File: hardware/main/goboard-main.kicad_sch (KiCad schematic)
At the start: 12 parts, among them J1 USB_C_Receptacle_USB2.0, J2 Conn_02x05_Top_Bottom, J3 Conn_01x01, J4 Conn_01x04, SW11 SW_Push

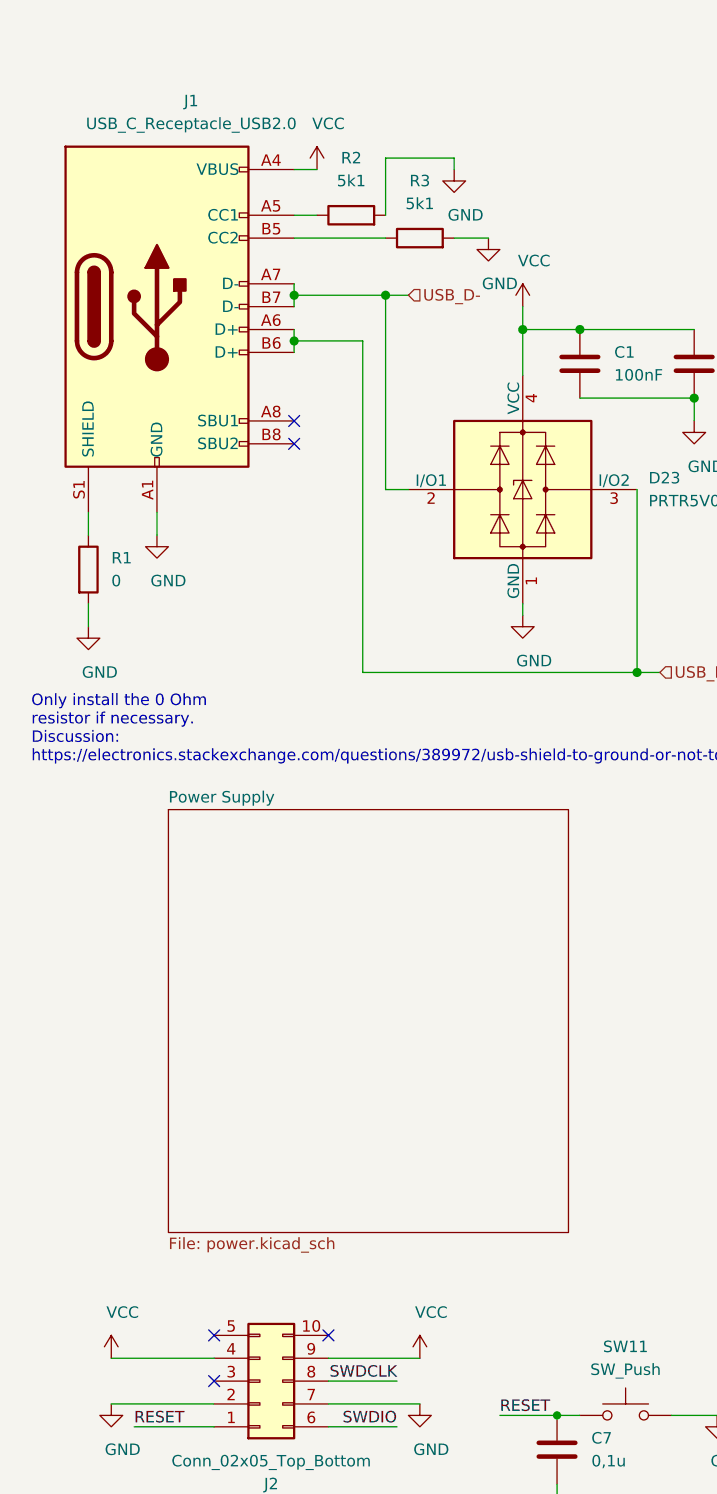
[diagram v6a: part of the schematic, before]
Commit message: Add power supply from the debugging connector
The batteries have to be disconnected when the debugger is plugged in,
as the voltages differ (ca. 2V for the batteries, 3.3V for the
debugger).
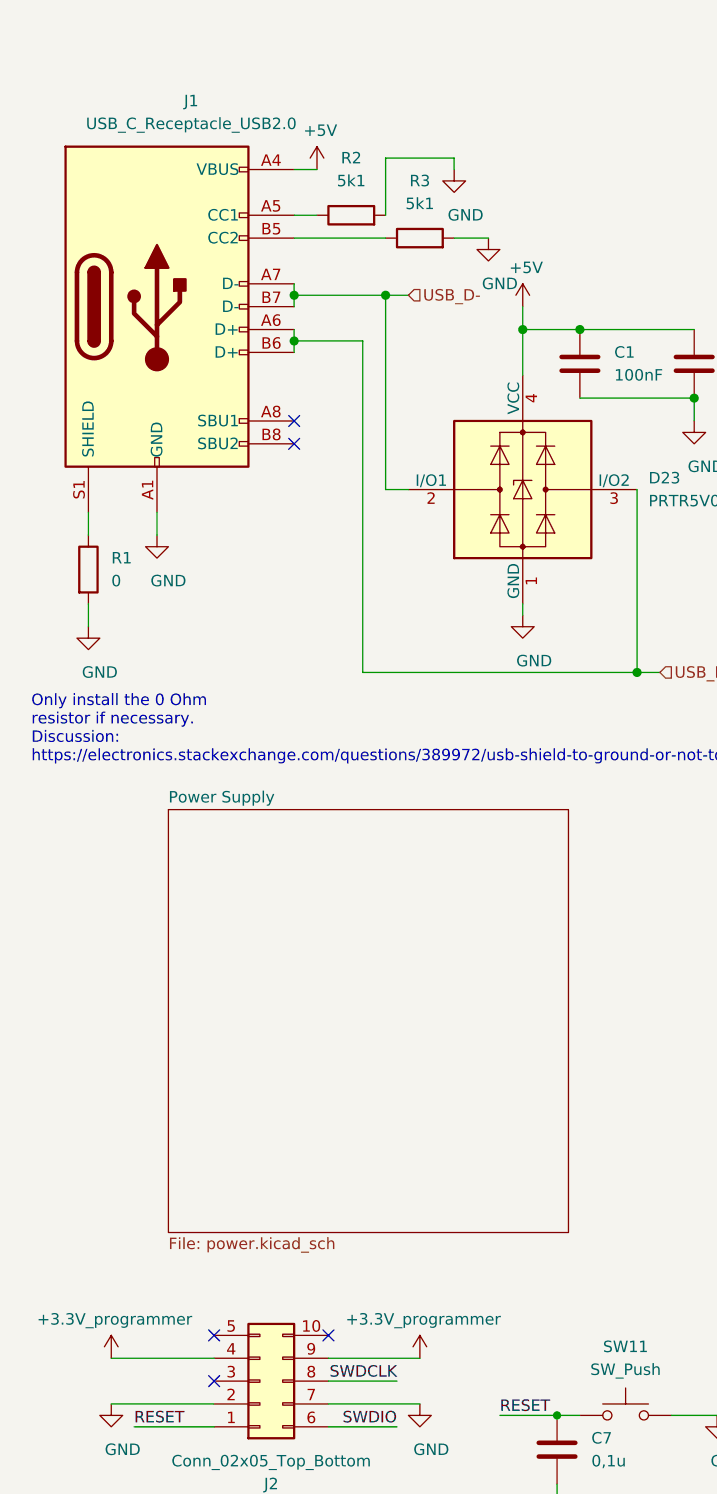
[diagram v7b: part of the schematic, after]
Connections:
- net VCC renamed +5V
- net +5V: no longer J2.4 (Pin_4), J2.9 (Pin_9)
- new net +3V3: J2.4 (Pin_4), J2.9 (Pin_9)
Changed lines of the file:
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@@
   (junction (at 80.01 91.44) (diameter 1.016) (color 0 0 0 0))
   (junction (at 86.36 60.96) (diameter 1.016) (color 0 0 0 0))
+  (no_connect (at 33.02 165.1))
+  (no_connect (at 33.02 170.18))
+  (no_connect (at 41.91 63.5))
   (no_connect (at 41.91 66.04))
   (no_connect (at 45.72 165.1))
-  (no_connect (at 41.91 63.5))
-  (no_connect (at 33.02 170.18))
-  (no_connect (at 33.02 165.1))
   (wire (pts (xy 19.05 73.66) (xy 19.05 76.2))
     (stroke (width 0) (type solid) (color 0 0 0 0))
@@
     (effects (font (size 1.27 1.27)) (justify right))
   )
-  (symbol (lib_id "power:VCC") (at 21.59 167.64 0) (unit 1)
-    (in_bom yes) (on_board yes)
-    (property "Reference" "#PWR0115" (id 0) (at 21.59 171.45 0)
-      (effects (font (size 1.27 1.27)) hide)
-    )
-    (property "Value" "VCC" (id 1) (at 22.86 162.56 0))
+  (symbol (lib_id "power:+3.3V") (at 21.59 167.64 0) (unit 1)
+    (in_bom yes) (on_board yes)
+    (property "Reference" "#PWR?" (id 0) (at 21.59 171.45 0)
+      (effects (font (size 1.27 1.27)) hide)
+    )
+    (property "Value" "+3.3V_programmer" (id 1) (at 21.958 163.316 0))
     (property "Footprint" "" (id 2) (at 21.59 167.64 0)
       (effects (font (size 1.27 1.27)) hide)
@@
     )
   )
-  (symbol (lib_id "power:VCC") (at 44.45 35.56 0) (unit 1)
-    (in_bom yes) (on_board yes)
-    (property "Reference" "#PWR0108" (id 0) (at 44.45 39.37 0)
-      (effects (font (size 1.27 1.27)) hide)
-    )
-    (property "Value" "VCC" (id 1) (at 45.72 30.48 0))
+  (symbol (lib_id "power:+5V") (at 44.45 35.56 0) (unit 1)
+    (in_bom yes) (on_board yes)
+    (property "Reference" "#PWR?" (id 0) (at 44.45 39.37 0)
+      (effects (font (size 1.27 1.27)) hide)
+    )
+    (property "Value" "+5V" (id 1) (at 44.8183 31.2356 0))
     (property "Footprint" "" (id 2) (at 44.45 35.56 0)
       (effects (font (size 1.27 1.27)) hide)
@@
     )
   )
-  (symbol (lib_id "power:VCC") (at 55.88 167.64 0) (unit 1)
-    (in_bom yes) (on_board yes)
-    (property "Reference" "#PWR0116" (id 0) (at 55.88 171.45 0)
-      (effects (font (size 1.27 1.27)) hide)
-    )
-    (property "Value" "VCC" (id 1) (at 57.15 162.56 0))
+  (symbol (lib_id "power:+3.3V") (at 55.88 167.64 0) (unit 1)
+    (in_bom yes) (on_board yes)
+    (property "Reference" "#PWR?" (id 0) (at 55.88 171.45 0)
+      (effects (font (size 1.27 1.27)) hide)
+    )
+    (property "Value" "+3.3V_programmer" (id 1) (at 56.248 163.316 0))
     (property "Footprint" "" (id 2) (at 55.88 167.64 0)
       (effects (font (size 1.27 1.27)) hide)
@@
     )
   )
-  (symbol (lib_id "power:VCC") (at 67.31 50.8 0) (unit 1)
-    (in_bom yes) (on_board yes)
-    (property "Reference" "#PWR0105" (id 0) (at 67.31 54.61 0)
-      (effects (font (size 1.27 1.27)) hide)
-    )
-    (property "Value" "VCC" (id 1) (at 68.58 45.72 0))
+  (symbol (lib_id "power:+5V") (at 67.31 50.8 0) (unit 1)
+    (in_bom yes) (on_board yes)
+    (property "Reference" "#PWR?" (id 0) (at 67.31 54.61 0)
+      (effects (font (size 1.27 1.27)) hide)
+    )
+    (property "Value" "+5V" (id 1) (at 67.6783 46.4756 0))
     (property "Footprint" "" (id 2) (at 67.31 50.8 0)
       (effects (font (size 1.27 1.27)) hide)
@@
       (reference "#PWR0104") (unit 1) (value "GND") (footprint "")
     )
-    (path "/10d1edb8-8b29-4fe3-a555-75b162cdbe50"
-      (reference "#PWR0105") (unit 1) (value "VCC") (footprint "")
-    )
     (path "/b191cc59-bae4-4339-8da5-2ddb0f841454"
       (reference "#PWR0106") (unit 1) (value "GND") (footprint "")
@@
       (reference "#PWR0107") (unit 1) (value "GND") (footprint "")
     )
-    (path "/1b8c8e34-d65d-4104-adb7-100f01a2586c"
-      (reference "#PWR0108") (unit 1) (value "VCC") (footprint "")
-    )
     (path "/3cca0c92-7d8e-49df-9010-76c61e46cb74"
       (reference "#PWR0114") (unit 1) (value "GND") (footprint "")
     )
-    (path "/e1a5293e-3487-44e5-9f3a-714fd6e7f88c"
-      (reference "#PWR0115") (unit 1) (value "VCC") (footprint "")
-    )
-    (path "/5d8ac5ba-d12b-49f1-8a83-545757fd38e6"
-      (reference "#PWR0116") (unit 1) (value "VCC") (footprint "")
-    )
     (path "/75356a8b-36c6-4cab-8e48-aa1d13fe71cb"
       (reference "#PWR0117") (unit 1) (value "GND") (footprint "")
@@
       (reference "#PWR0120") (unit 1) (value "GND") (footprint "")
     )
+    (path "/07811baa-5fc4-44cf-bdf3-f2a2052932c3"
+      (reference "#PWR?") (unit 1) (value "+3.3V_programmer") (footprint "")
+    )
+    (path "/3d3f8e2a-f865-4816-a544-ca3d0200d21e"
+      (reference "#PWR?") (unit 1) (value "+5V") (footprint "")
+    )
+    (path "/bc0831f1-3f1a-47cb-9568-da9cd7dc366c"
+      (reference "#PWR?") (unit 1) (value "+3.3V_programmer") (footprint "")
+    )
+    (path "/e6e7b860-7cfe-4dac-95d7-4e581f04437d"
+      (reference "#PWR?") (unit 1) (value "+5V") (footprint "")
+    )
     (path "/d7e33325-4578-4e92-bf2f-a87bebb610ba"
       (reference "C1") (unit 1) (value "100nF") (footprint "Capacitor_SMD:C_0201_0603Metric_Pad0.64x0.40mm_HandSolder")
@@
       (reference "U4") (unit 1) (value "74LV165") (footprint "Package_SO:TSSOP-16_4.4x5mm_P0.65mm")
     )
-  )
+    (path "/a2ebbcc0-d455-4794-9fcf-d50cef56d65b/513f966b-4495-4990-b182-5526dff63093"
+      (reference "#PWR?") (unit 1) (value "+3.3V_programmer") (footprint "")
+    )
+    (path "/a2ebbcc0-d455-4794-9fcf-d50cef56d65b/84df1307-86f3-47b4-a1aa-8cb15884156f"
+      (reference "#PWR?") (unit 1) (value "+BATT") (footprint "")
+    )
+    (path "/a2ebbcc0-d455-4794-9fcf-d50cef56d65b/b948eed3-787f-47a4-8871-24e51a945e2e"
+      (reference "#PWR?") (unit 1) (value "+5V") (footprint "")
+    )
+    (path "/a2ebbcc0-d455-4794-9fcf-d50cef56d65b/fcf91b1c-89df-48d3-a079-670ff776b9bc"
+      (reference "#PWR?") (unit 1) (value "GND") (footprint "")
+    )
+    (path "/a2ebbcc0-d455-4794-9fcf-d50cef56d65b/210515f0-c0f1-4f80-b920-f3ce9df10676"
+      (reference "BT?") (unit 1) (value "Battery") (footprint "")
+    )
+    (path "/a2ebbcc0-d455-4794-9fcf-d50cef56d65b/eda3ac85-180c-4149-a69c-6ee2b133cab0"
+      (reference "BT?") (unit 1) (value "Battery") (footprint "")
+    )
+    (path "/a2ebbcc0-d455-4794-9fcf-d50cef56d65b/d97a629e-f5e3-4e10-a29b-be0ad1d5f5ac"
+      (reference "D?") (unit 1) (value "DIODE") (footprint "")
+    )
+    (path "/a2ebbcc0-d455-4794-9fcf-d50cef56d65b/f0252d66-95ed-4e48-8ba2-5d7673eeffb0"
+      (reference "Q?") (unit 1) (value "Q_PMOS_DGS") (footprint "")
+    )
+    (path "/a2ebbcc0-d455-4794-9fcf-d50cef56d65b/94b1480c-21b6-4ef7-b592-3977ba8ffc39"
+      (reference "R?") (unit 1) (value "R") (footprint "")
+    )
+  )

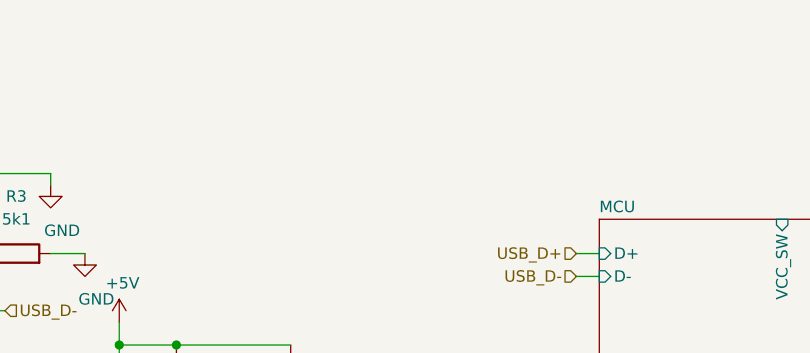
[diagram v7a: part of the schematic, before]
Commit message: Add new board outline
Reason: This makes the first design iteration of the case possible.
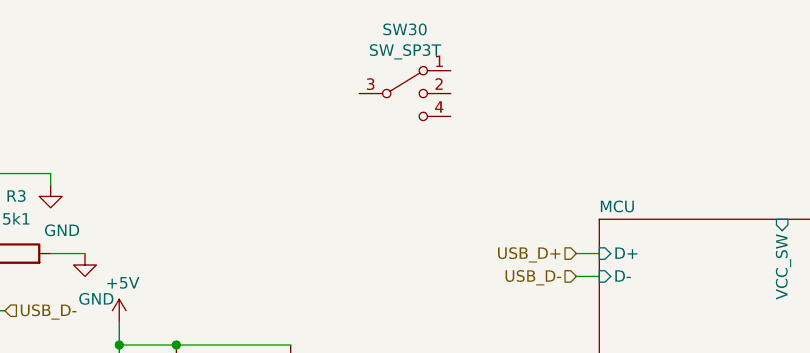
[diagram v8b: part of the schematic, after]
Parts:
- added SW30: SW_SP3T, Connector_PinHeader_2.54mm:PinHeader_1x05_P2.54mm_Vertical, symbol Switch:SW_SP3T
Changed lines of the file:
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@@
   (symbol (lib_id "power:+3.3V") (at 21.59 167.64 0) (unit 1)
     (in_bom yes) (on_board yes)
-    (property "Reference" "#PWR?" (id 0) (at 21.59 171.45 0)
+    (property "Reference" "#PWR0108" (id 0) (at 21.59 171.45 0)
       (effects (font (size 1.27 1.27)) hide)
     )
@@
   (symbol (lib_id "power:+5V") (at 44.45 35.56 0) (unit 1)
     (in_bom yes) (on_board yes)
-    (property "Reference" "#PWR?" (id 0) (at 44.45 39.37 0)
+    (property "Reference" "#PWR0116" (id 0) (at 44.45 39.37 0)
       (effects (font (size 1.27 1.27)) hide)
     )
@@
   (symbol (lib_id "power:+3.3V") (at 55.88 167.64 0) (unit 1)
     (in_bom yes) (on_board yes)
-    (property "Reference" "#PWR?" (id 0) (at 55.88 171.45 0)
+    (property "Reference" "#PWR0105" (id 0) (at 55.88 171.45 0)
       (effects (font (size 1.27 1.27)) hide)
     )
@@
   (symbol (lib_id "power:+5V") (at 67.31 50.8 0) (unit 1)
     (in_bom yes) (on_board yes)
-    (property "Reference" "#PWR?" (id 0) (at 67.31 54.61 0)
+    (property "Reference" "#PWR0115" (id 0) (at 67.31 54.61 0)
       (effects (font (size 1.27 1.27)) hide)
     )
@@
     )
     (property "Datasheet" "~" (id 3) (at 265.43 134.62 0)
+      (effects (font (size 1.27 1.27)) hide)
+    )
+  )
+  (symbol (lib_id "Switch:SW_SP3T") (at 99.06 25.4 0) (unit 1)
+    (in_bom yes) (on_board yes)
+    (property "Reference" "SW30" (id 0) (at 99.06 18.3196 0))
+    (property "Value" "SW_SP3T" (id 1) (at 99.06 20.6183 0))
+    (property "Footprint" "Connector_PinHeader_2.54mm:PinHeader_1x05_P2.54mm_Vertical" (id 2) (at 83.185 20.955 0)
+      (effects (font (size 1.27 1.27)) hide)
+    )
+    (property "Datasheet" "~" (id 3) (at 83.185 20.955 0)
       (effects (font (size 1.27 1.27)) hide)
     )
@@
       (reference "#PWR0104") (unit 1) (value "GND") (footprint "")
     )
+    (path "/07811baa-5fc4-44cf-bdf3-f2a2052932c3"
+      (reference "#PWR0105") (unit 1) (value "+3.3V_programmer") (footprint "")
+    )
     (path "/b191cc59-bae4-4339-8da5-2ddb0f841454"
       (reference "#PWR0106") (unit 1) (value "GND") (footprint "")
@@
       (reference "#PWR0107") (unit 1) (value "GND") (footprint "")
     )
+    (path "/bc0831f1-3f1a-47cb-9568-da9cd7dc366c"
+      (reference "#PWR0108") (unit 1) (value "+3.3V_programmer") (footprint "")
+    )
     (path "/3cca0c92-7d8e-49df-9010-76c61e46cb74"
       (reference "#PWR0114") (unit 1) (value "GND") (footprint "")
     )
+    (path "/3d3f8e2a-f865-4816-a544-ca3d0200d21e"
+      (reference "#PWR0115") (unit 1) (value "+5V") (footprint "")
+    )
+    (path "/e6e7b860-7cfe-4dac-95d7-4e581f04437d"
+      (reference "#PWR0116") (unit 1) (value "+5V") (footprint "")
+    )
     (path "/75356a8b-36c6-4cab-8e48-aa1d13fe71cb"
       (reference "#PWR0117") (unit 1) (value "GND") (footprint "")
@@
       (reference "#PWR0120") (unit 1) (value "GND") (footprint "")
     )
-    (path "/07811baa-5fc4-44cf-bdf3-f2a2052932c3"
-      (reference "#PWR?") (unit 1) (value "+3.3V_programmer") (footprint "")
-    )
-    (path "/3d3f8e2a-f865-4816-a544-ca3d0200d21e"
-      (reference "#PWR?") (unit 1) (value "+5V") (footprint "")
-    )
-    (path "/bc0831f1-3f1a-47cb-9568-da9cd7dc366c"
-      (reference "#PWR?") (unit 1) (value "+3.3V_programmer") (footprint "")
-    )
-    (path "/e6e7b860-7cfe-4dac-95d7-4e581f04437d"
-      (reference "#PWR?") (unit 1) (value "+5V") (footprint "")
-    )
     (path "/d7e33325-4578-4e92-bf2f-a87bebb610ba"
       (reference "C1") (unit 1) (value "100nF") (footprint "Capacitor_SMD:C_0201_0603Metric_Pad0.64x0.40mm_HandSolder")
@@
       (reference "SW11") (unit 1) (value "SW_Push") (footprint "")
     )
+    (path "/574bf794-a392-40ef-97b7-11f07d51473e"
+      (reference "SW30") (unit 1) (value "SW_SP3T") (footprint "Connector_PinHeader_2.54mm:PinHeader_1x05_P2.54mm_Vertical")
+    )
     (path "/d1d7b976-c206-4a6a-bf43-9e0a3d3fc0a5/30c2ac1c-8a76-41a0-94de-8ad0d2ee7b5a"
       (reference "#PWR0109") (unit 1) (value "GND") (footprint "")
@@
       (reference "U4") (unit 1) (value "74LV165") (footprint "Package_SO:TSSOP-16_4.4x5mm_P0.65mm")
     )
+    (path "/a2ebbcc0-d455-4794-9fcf-d50cef56d65b/84df1307-86f3-47b4-a1aa-8cb15884156f"
+      (reference "#PWR0125") (unit 1) (value "+BATT") (footprint "")
+    )
     (path "/a2ebbcc0-d455-4794-9fcf-d50cef56d65b/513f966b-4495-4990-b182-5526dff63093"
-      (reference "#PWR?") (unit 1) (value "+3.3V_programmer") (footprint "")
-    )
-    (path "/a2ebbcc0-d455-4794-9fcf-d50cef56d65b/84df1307-86f3-47b4-a1aa-8cb15884156f"
-      (reference "#PWR?") (unit 1) (value "+BATT") (footprint "")
+      (reference "#PWR0126") (unit 1) (value "+3.3V_programmer") (footprint "")
     )
     (path "/a2ebbcc0-d455-4794-9fcf-d50cef56d65b/b948eed3-787f-47a4-8871-24e51a945e2e"
-      (reference "#PWR?") (unit 1) (value "+5V") (footprint "")
+      (reference "#PWR0127") (unit 1) (value "+5V") (footprint "")
     )
     (path "/a2ebbcc0-d455-4794-9fcf-d50cef56d65b/fcf91b1c-89df-48d3-a079-670ff776b9bc"
-      (reference "#PWR?") (unit 1) (value "GND") (footprint "")
+      (reference "#PWR0128") (unit 1) (value "GND") (footprint "")
     )
     (path "/a2ebbcc0-d455-4794-9fcf-d50cef56d65b/210515f0-c0f1-4f80-b920-f3ce9df10676"
-      (reference "BT?") (unit 1) (value "Battery") (footprint "")
+      (reference "BT1") (unit 1) (value "Battery") (footprint "")
     )
     (path "/a2ebbcc0-d455-4794-9fcf-d50cef56d65b/eda3ac85-180c-4149-a69c-6ee2b133cab0"
-      (reference "BT?") (unit 1) (value "Battery") (footprint "")
+      (reference "BT2") (unit 1) (value "Battery") (footprint "")
     )
     (path "/a2ebbcc0-d455-4794-9fcf-d50cef56d65b/d97a629e-f5e3-4e10-a29b-be0ad1d5f5ac"
-      (reference "D?") (unit 1) (value "DIODE") (footprint "")
+      (reference "D48") (unit 1) (value "DIODE") (footprint "")
     )
     (path "/a2ebbcc0-d455-4794-9fcf-d50cef56d65b/f0252d66-95ed-4e48-8ba2-5d7673eeffb0"
-      (reference "Q?") (unit 1) (value "Q_PMOS_DGS") (footprint "")
+      (reference "Q1") (unit 1) (value "Q_PMOS_DGS") (footprint "")
     )
     (path "/a2ebbcc0-d455-4794-9fcf-d50cef56d65b/94b1480c-21b6-4ef7-b592-3977ba8ffc39"
-      (reference "R?") (unit 1) (value "R") (footprint "")
-    )
-  )
+      (reference "R7") (unit 1) (value "R") (footprint "")
+    )
+  )
